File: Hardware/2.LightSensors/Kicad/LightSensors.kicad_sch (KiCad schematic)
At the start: 7 parts, among them U1 AS7331

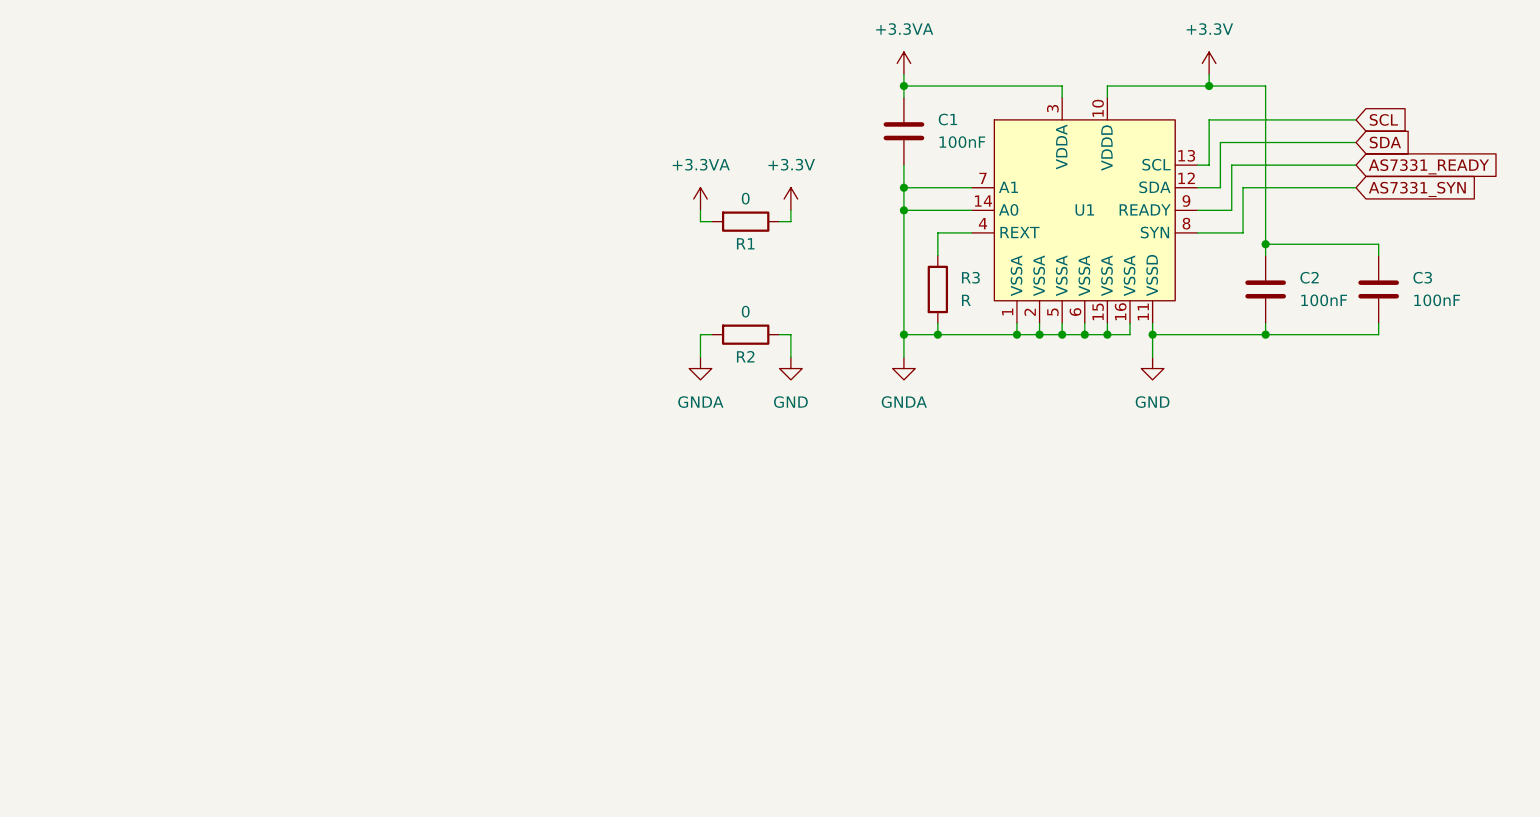
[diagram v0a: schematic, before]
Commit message: Add OPT3004 into schematic
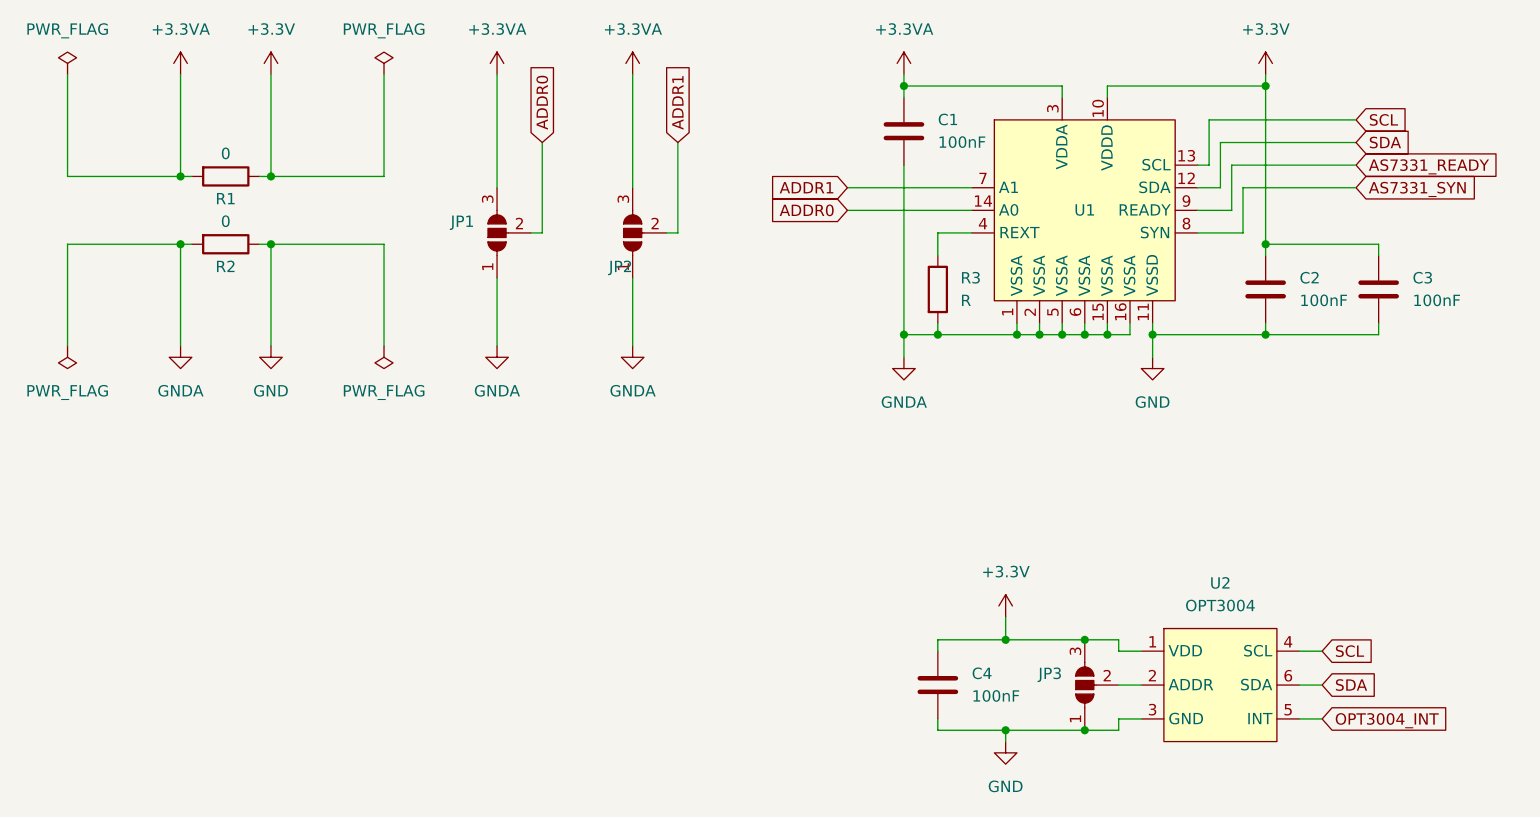
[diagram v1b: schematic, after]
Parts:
- added C4: 100nF, Capacitor_SMD:C_0402_1005Metric, symbol Device:C
- added JP1, JP2, JP3: SolderJumper_3_Open, symbol Jumper:SolderJumper_3_Open
- added U2: OPT3004, symbol Sensor_Light_OPT3004:OPT3004
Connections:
- net +3.3V: now also C4.1, JP3.3 (B), U2.1 (VDD)
- net +3.3VA: now also JP1.3 (B), JP2.3 (B)
- net GND: now also C4.2, JP3.1 (A), U2.3 (GND)
- net GNDA: now also JP1.1 (A), JP2.1 (A); no longer U1.14 (A0), U1.7 (A1)
- net SCL: now also U2.4 (SCL)
- net SDA: now also U2.6 (SDA)
- new net: JP3.2 (C), U2.2 (ADDR)
- new net ADDR0: JP1.2 (C), U1.14 (A0)
- new net ADDR1: JP2.2 (C), U1.7 (A1)
- new net OPT3004_INT: U2.5 (INT)
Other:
- moved on the sheet: R1, R2

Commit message: Assign footprints
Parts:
- JP1, JP2, JP3: footprint (none) -> Jumper:SolderJumper-3_P2.0mm_Open_TrianglePad1.0x1.5mm
- U2: footprint (none) -> OPT3004:SON65P200X200X65-7N
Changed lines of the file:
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@@
       (effects (font (size 1.27 1.27)) (justify left) hide)
     )
-    (property "Footprint" "" (at 87.63 50.8 0)
+    (property "Footprint" "Jumper:SolderJumper-3_P2.0mm_Open_TrianglePad1.0x1.5mm" (at 87.63 50.8 0)
       (effects (font (size 1.27 1.27)) hide)
     )
@@
       (effects (font (size 1.27 1.27)) (justify left) hide)
     )
-    (property "Footprint" "" (at 138.43 101.6 0)
+    (property "Footprint" "Jumper:SolderJumper-3_P2.0mm_Open_TrianglePad1.0x1.5mm" (at 138.43 101.6 0)
       (effects (font (size 1.27 1.27)) hide)
     )
@@
       (effects (font (size 1.27 1.27)) (justify left) hide)
     )
-    (property "Footprint" "" (at 72.39 50.8 0)
+    (property "Footprint" "Jumper:SolderJumper-3_P2.0mm_Open_TrianglePad1.0x1.5mm" (at 72.39 50.8 0)
       (effects (font (size 1.27 1.27)) hide)
     )
@@
       (effects (font (size 1.27 1.27)))
     )
-    (property "Footprint" "" (at 153.67 101.6 0)
-      (effects (font (size 1.27 1.27)) hide)
-    )
+    (property "Footprint" "OPT3004:SON65P200X200X65-7N" (at 153.67 101.6 0)
+      (effects (font (size 1.27 1.27)) hide)
+    )

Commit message: Update schematic
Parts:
- added R4, R5, R6: 10K, Capacitor_SMD:C_0402_1005Metric, symbol Device:R
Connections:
- net +3.3V: now also R4.1, R5.1, R6.1
- net OPT3004_INT: now also R6.2
- net SCL: now also R4.2
- net SDA: now also R5.2
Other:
- note added: "0x44 - ADDR->GND 0x45 - ADDR->VCC 0x46 - ADDR->SDA 0x47 - ADDR->SCL"
- note added: "0x74 - 0 and 0 0x75 - 0 and 1 0x76 - 1 and 0 0x77 - 1 and 1"
- moved on the sheet: C1, C2, C3, C4, JP1, JP2, JP3, R1, R2, R3, U1, U2

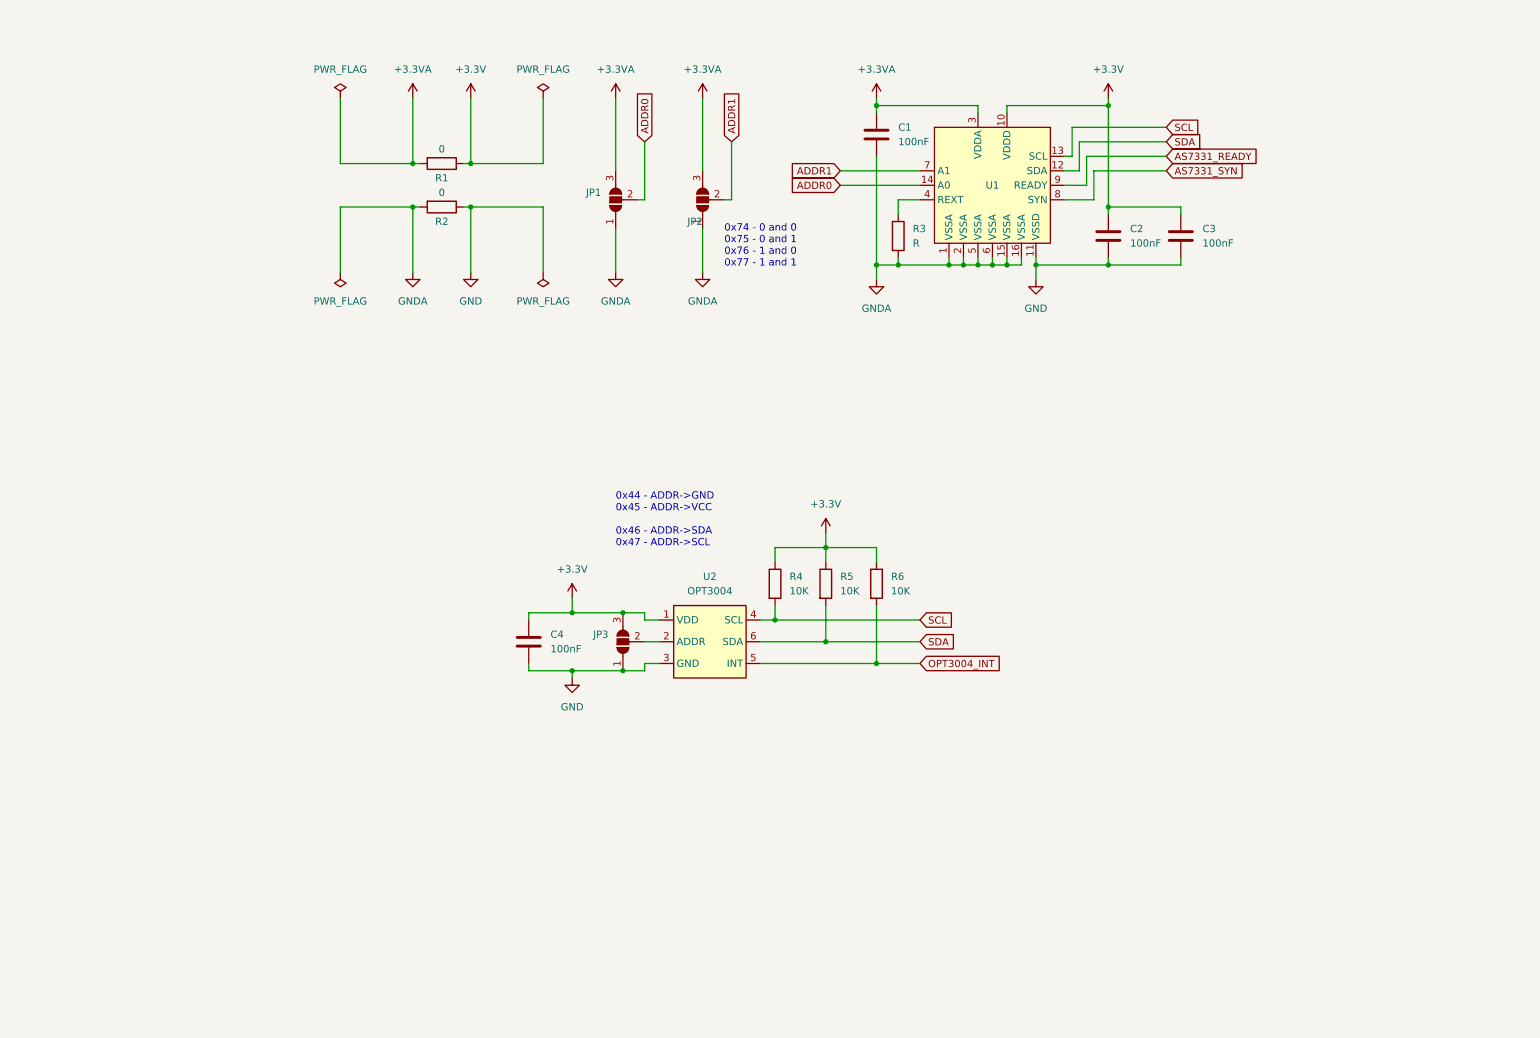
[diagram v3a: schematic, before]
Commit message: Update schematic for LightSensors PCB
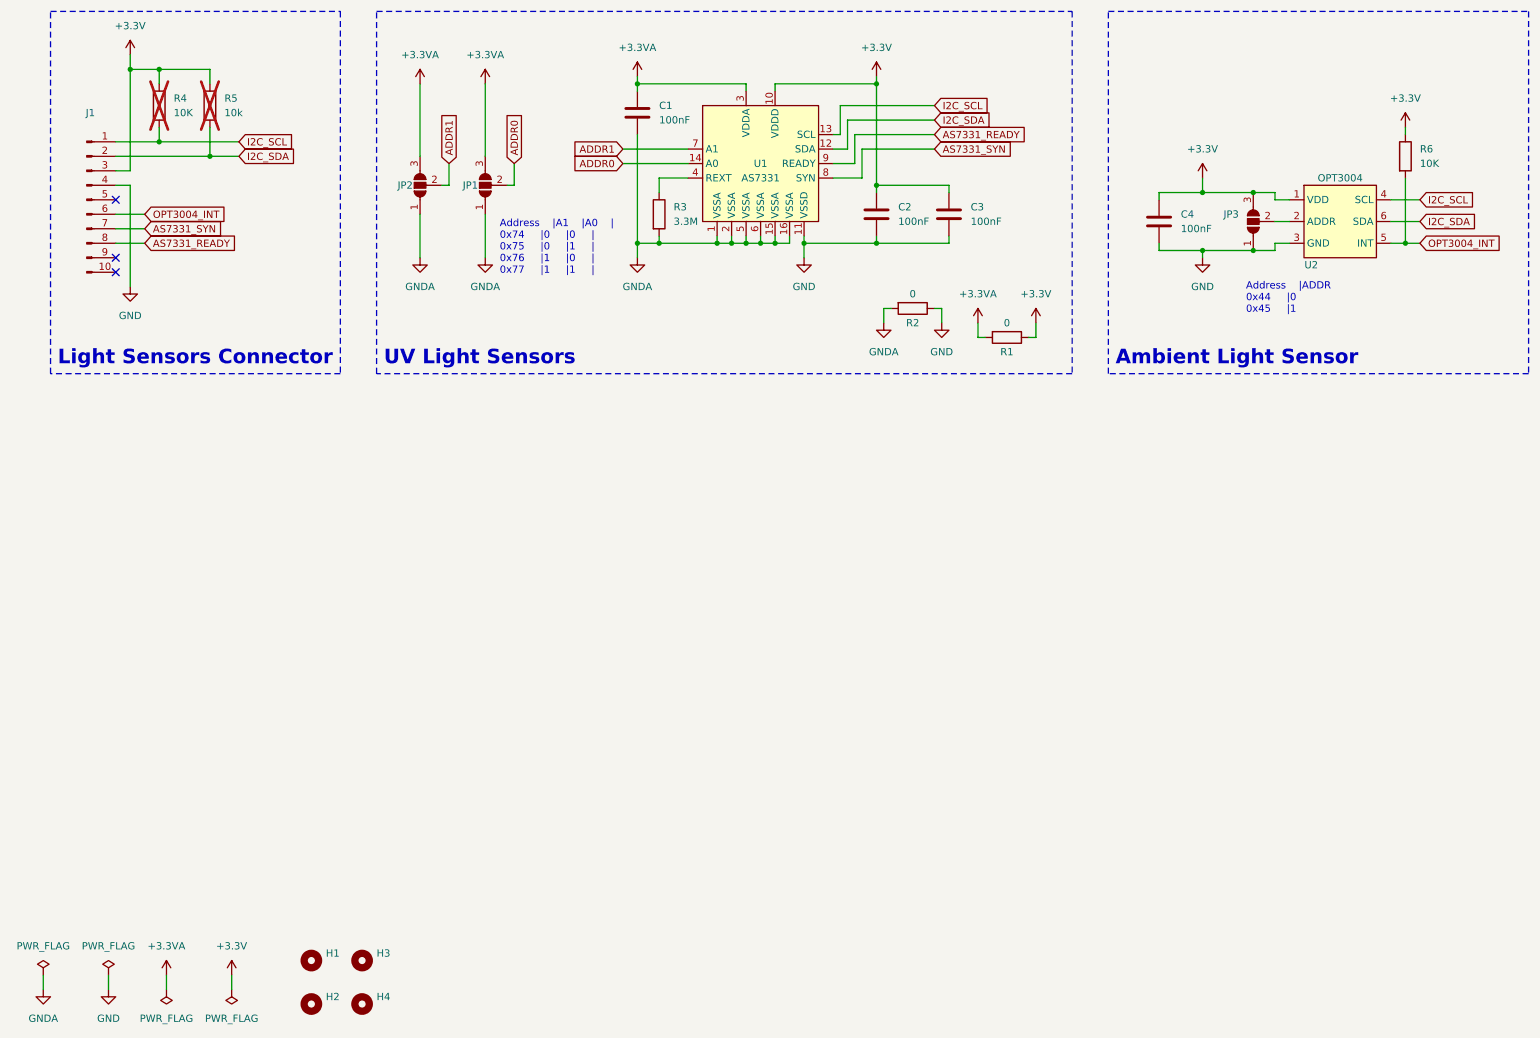
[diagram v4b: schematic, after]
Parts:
- added H1, H2, H3, H4: MountingHole, MountingHole:MountingHole_3.2mm_M3_ISO7380, symbol Mechanical:MountingHole
- added J1: Conn_01x10_Pin, Connector_PinHeader_1.27mm:PinHeader_1x10_P1.27mm_Horizontal, symbol Connector:Conn_01x10_Pin
- R3: value R -> 3.3M
- R4: footprint Capacitor_SMD:C_0402_1005Metric -> Resistor_SMD:R_0402_1005Metric; now not fitted
- R5: value 10K -> 10k; footprint Capacitor_SMD:C_0402_1005Metric -> Resistor_SMD:R_0402_1005Metric; now not fitted
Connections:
- net +3.3V: now also J1.3 (Pin_3)
- net AS7331_READY: now also J1.8 (Pin_8)
- net AS7331_SYN: now also J1.7 (Pin_7)
- net GND: now also J1.4 (Pin_4)
- net OPT3004_INT: now also J1.6 (Pin_6)
- net SCL renamed I2C_SCL
- net I2C_SCL: now also J1.1 (Pin_1)
- net SDA renamed I2C_SDA
- net I2C_SDA: now also J1.2 (Pin_2)
- no-connect marks 0 -> 3
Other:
- note added: "Address |A1 |A0 | 0x74 |0 |0 | 0x75 |0 |1 | 0x76 |1 |0 | 0x77 |1 |1 |"
- note added: "Address |ADDR 0x44 |0 0x45 |1"
- note added: "Ambient Light Sensor"
- note added: "Light Sensors Connector"
- note added: "UV Light Sensors"
- note removed: "0x44 - ADDR->GND 0x45 - ADDR->VCC 0x46 - ADDR->SDA 0x47 - ADDR->SCL"
- note removed: "0x74 - 0 and 0 0x75 - 0 and 1 0x76 - 1 and 0 0x77 - 1 and 1"
- title: (none) -> LightSensors
- moved on the sheet: C1, C2, C3, C4, JP1, JP2, JP3, R1, R2, R3, R6, U1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

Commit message: Change connector to JST PH 2.0
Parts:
- J1: footprint Connector_PinHeader_1.27mm:PinHeader_1x10_P1.27mm_Horizontal -> Connector_JST:JST_PH_S10B-PH-K_1x10_P2.00mm_Horizontal
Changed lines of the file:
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@@
       (effects (font (size 1.27 1.27)) hide)
     )
-    (property "Footprint" "Connector_PinHeader_1.27mm:PinHeader_1x10_P1.27mm_Horizontal" (at 25.4 52.07 0)
+    (property "Footprint" "Connector_JST:JST_PH_S10B-PH-K_1x10_P2.00mm_Horizontal" (at 25.4 52.07 0)
       (effects (font (size 1.27 1.27)) hide)
     )
